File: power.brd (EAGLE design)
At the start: 83 x 56 mm, 22 parts

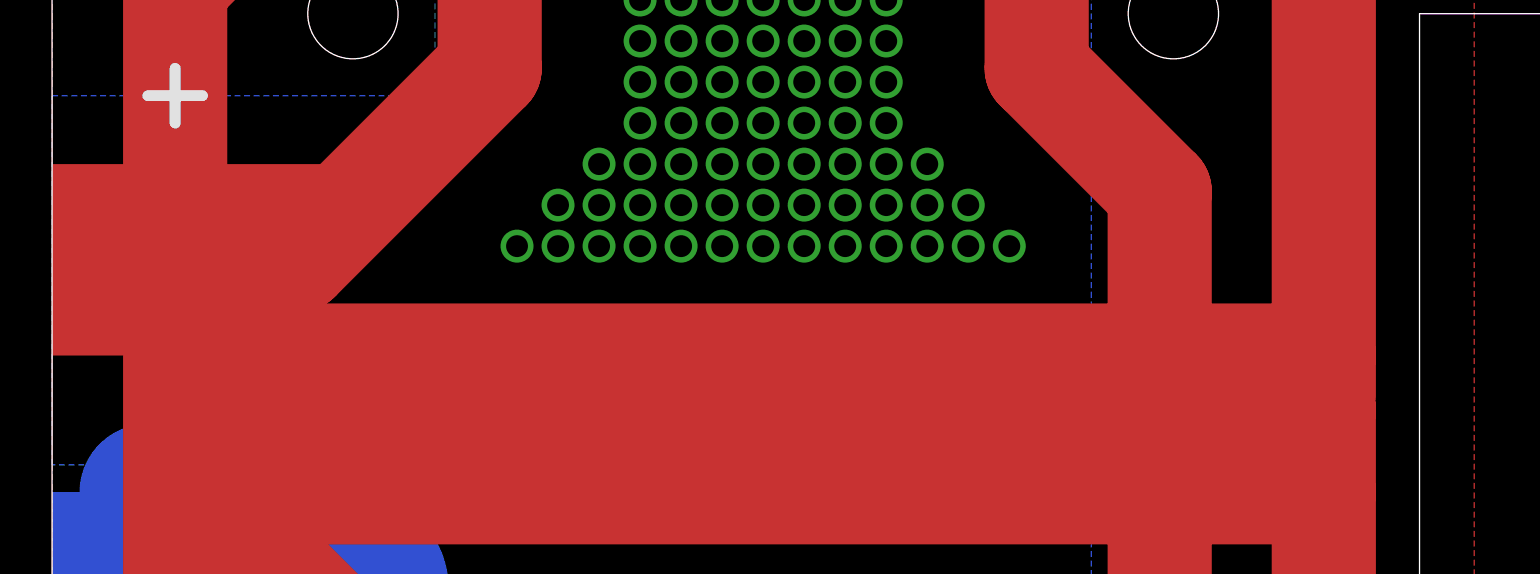
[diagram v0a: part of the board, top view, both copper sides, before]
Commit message: slightly refine power track
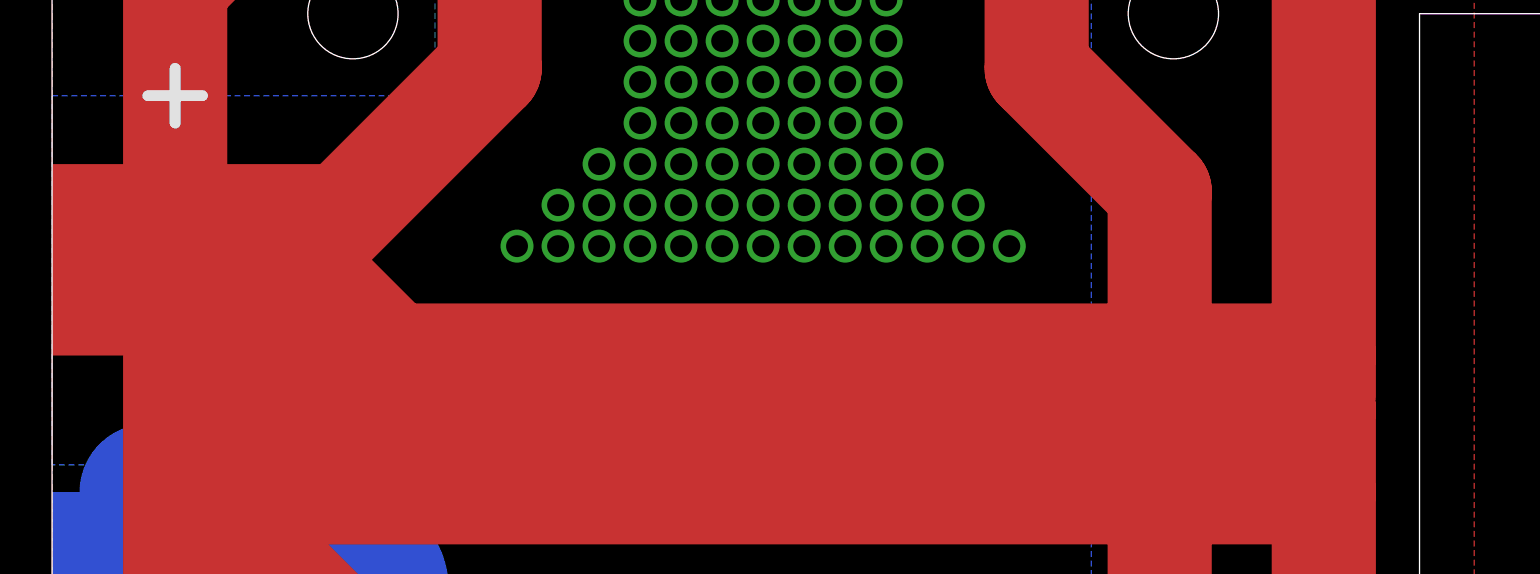
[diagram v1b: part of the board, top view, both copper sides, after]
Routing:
- net VIN: track 363.5 -> 370.5 mm
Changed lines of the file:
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@@
 <wire x1="46" y1="28" x2="40.5" y2="28" width="3.81" layer="1"/>
 <wire x1="10.5" y1="28" x2="5" y2="28" width="3.81" layer="1"/>
-<wire x1="46.5" y1="30.5" x2="6" y2="30.5" width="3.81" layer="1"/>
+<wire x1="46.5" y1="30.5" x2="12.5" y2="30.5" width="3.81" layer="1"/>
+<wire x1="12.5" y1="30.5" x2="6" y2="30.5" width="3.81" layer="1"/>
 <wire x1="46.5" y1="25.5" x2="6" y2="25.5" width="3.81" layer="1"/>
 <wire x1="4" y1="34" x2="4" y2="34.5" width="0.4064" layer="1"/>
+<wire x1="7.5" y1="35.5" x2="12.5" y2="30.5" width="3.81" layer="1"/>
 </signal>
 <signal name="GND">

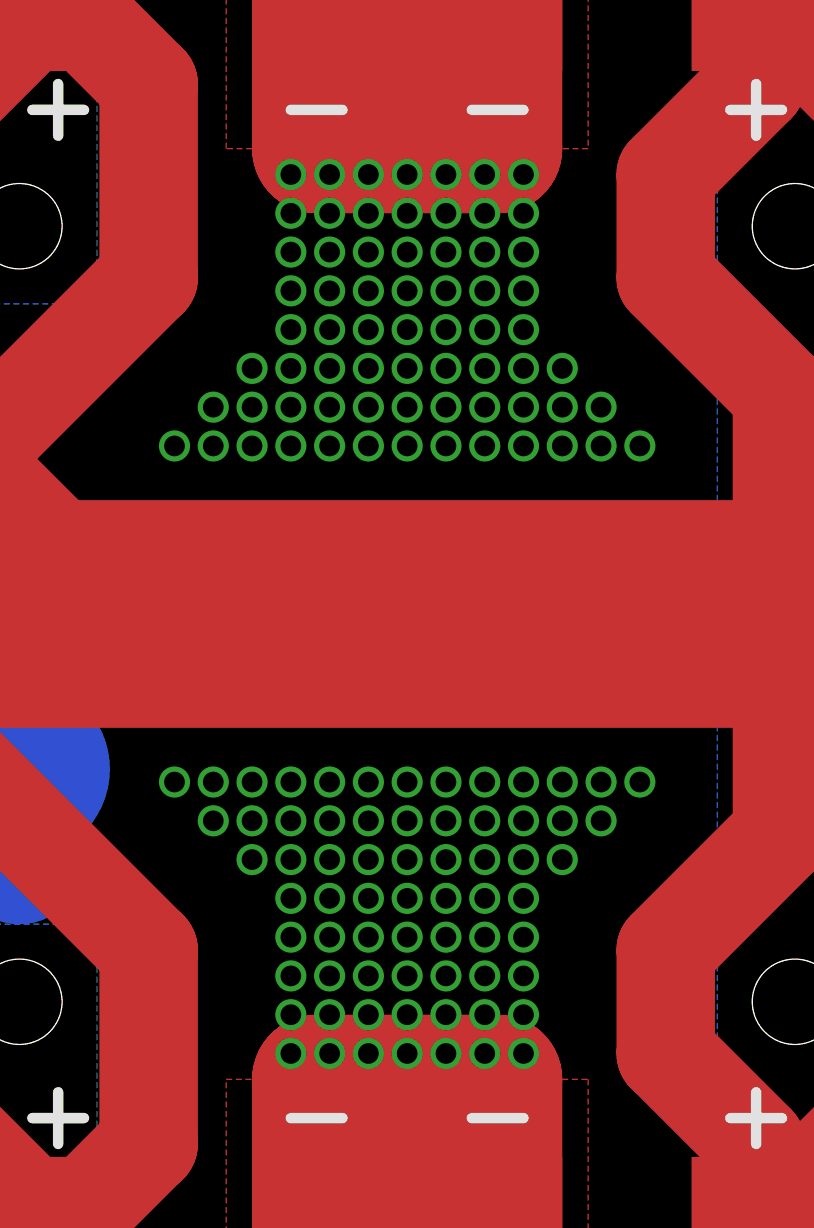
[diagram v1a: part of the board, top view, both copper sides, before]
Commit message: change drills
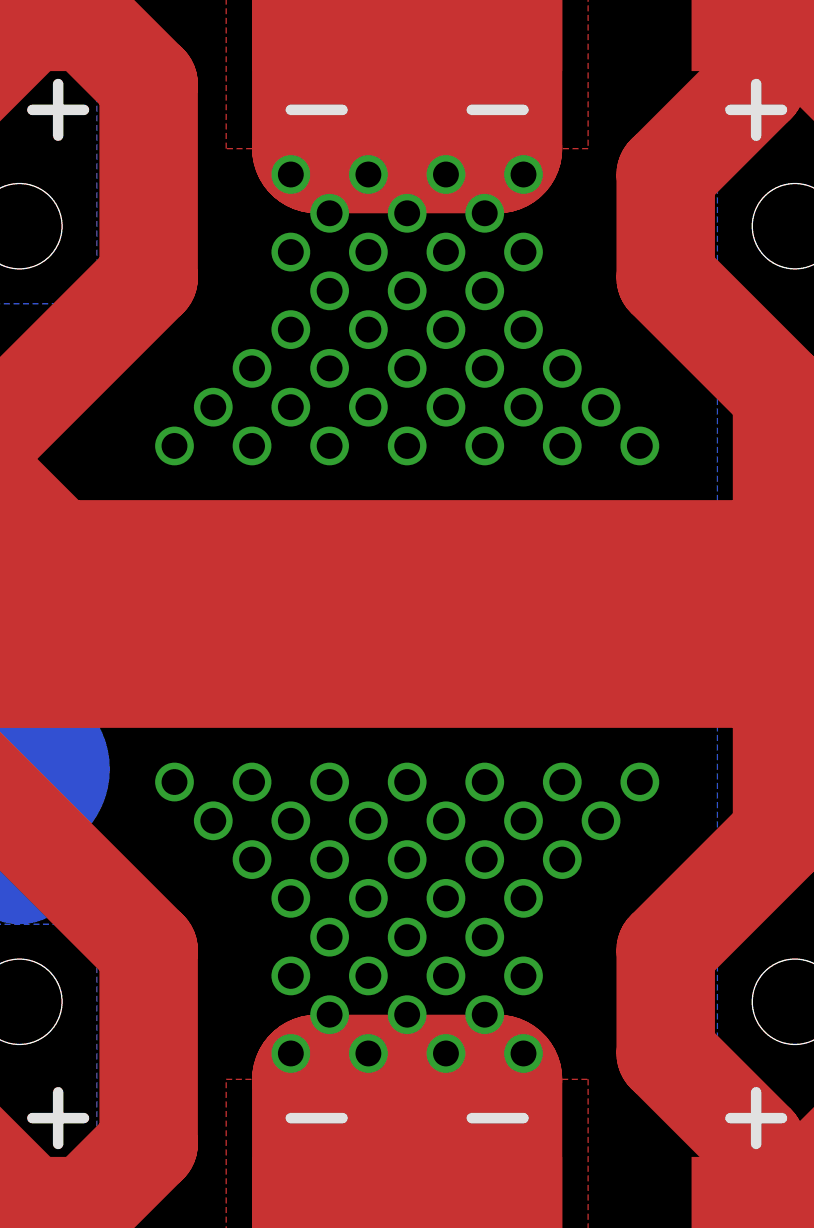
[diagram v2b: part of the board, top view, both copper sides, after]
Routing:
- net GND: vias 136 -> 72

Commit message: fix some positions
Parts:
- moved LOGO1 45.3 mm to (56.6, 50.5)
- moved STANDOFF5 8.00 mm to (19.0, 43.0)
- moved STANDOFF6 8.00 mm to (49.0, 13.0)
- moved STANDOFF7 8.00 mm to (19.0, 13.0)
- moved STANDOFF8 8.00 mm to (49.0, 43.0)
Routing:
- net VIN: track 370.5 -> 401.7 mm
- net GND: track 93.5 -> 75.4 mm, vias 72 -> 84
- net N$1: track 0.00 -> 10.5 mm
- net N$2: track 0.00 -> 10.0 mm
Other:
- outline, holes or cut-outs redrawn
